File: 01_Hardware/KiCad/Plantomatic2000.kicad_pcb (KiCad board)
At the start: 2 copper layers, 1 part, among them U1 ESP32-WROOM-32E

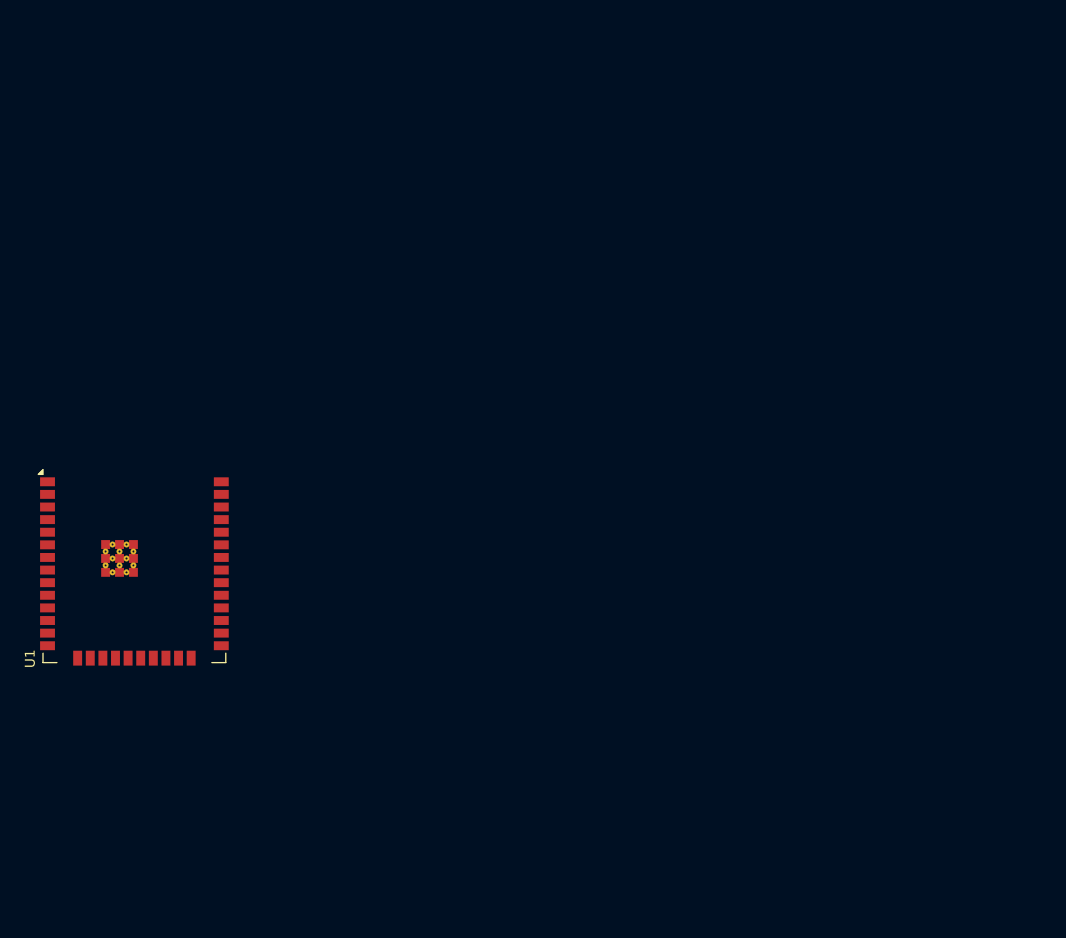
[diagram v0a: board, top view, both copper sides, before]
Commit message: Added foorptrints
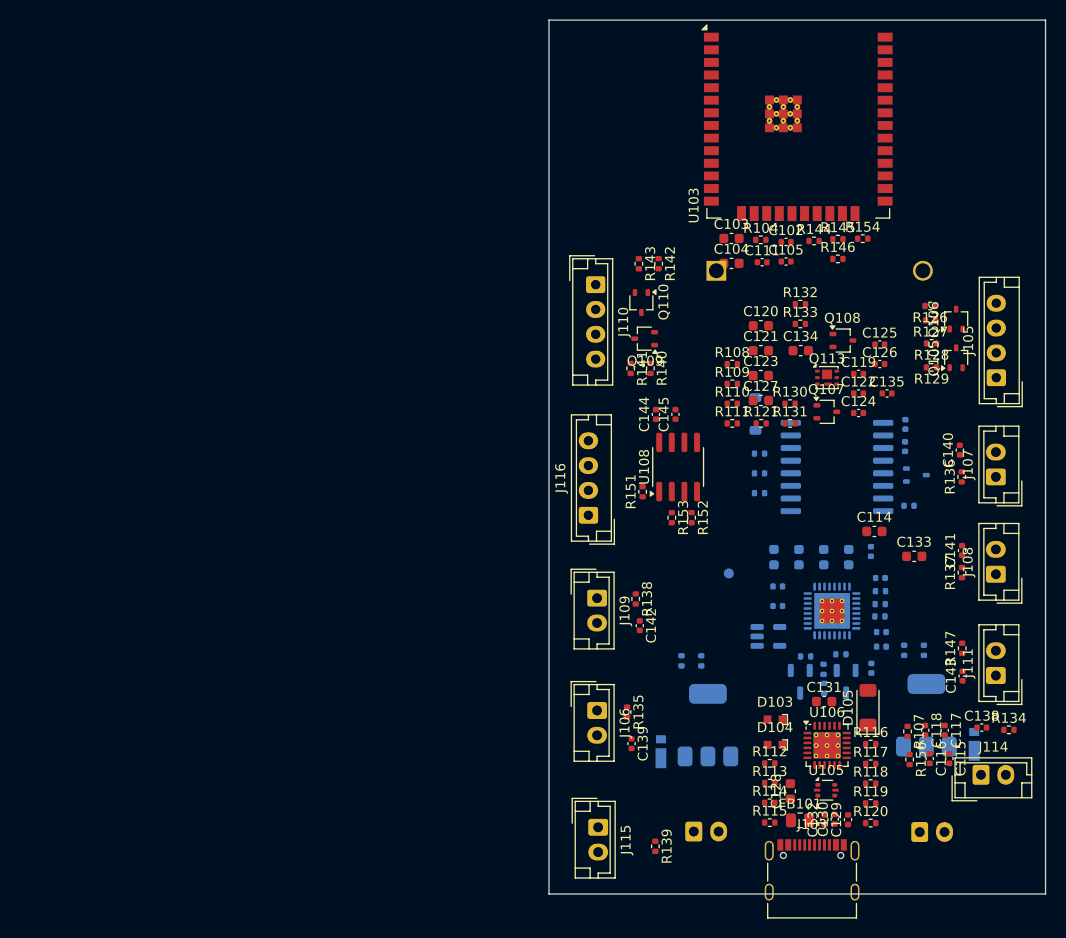
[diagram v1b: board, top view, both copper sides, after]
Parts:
- removed U1: ESP32-WROOM-32E, RF_Module:ESP32-WROOM-32E
- added BT101: Battery_Cell, Battery:BatteryHolder_MYOUNG_BS-07-A1BJ001_CR2032, B.Cu at (197.8, 66.2)
- added C101: 1uF, Capacitor_SMD:C_0402_1005Metric, B.Cu at (213.4, 94.5)
- added C102: 100nF, Capacitor_SMD:C_0402_1005Metric, F.Cu at (204.9, 63.3)
- added C103: 10uF, Capacitor_SMD:C_0603_1608Metric, F.Cu at (199.4, 63.0)
- added C104: 22uF, Capacitor_SMD:C_0603_1608Metric, F.Cu at (199.4, 65.5)
- added C105: 100nF, Capacitor_SMD:C_0402_1005Metric, F.Cu at (204.9, 65.3)
- added C106: 1uF, Capacitor_SMD:C_0402_1005Metric, B.Cu at (214.4, 97.2)
- added C107: 10uF, Capacitor_SMD:C_0603_1608Metric, B.Cu at (203.7, 95.1)
- added C108: 10uF, Capacitor_SMD:C_0603_1608Metric, B.Cu at (206.2, 95.1)
- added C109: 10uF, Capacitor_SMD:C_0603_1608Metric, B.Cu at (208.7, 95.1)
- added C110: 10uF, Capacitor_SMD:C_0603_1608Metric, B.Cu at (211.2, 95.1)
- added C111: 1uF, Capacitor_SMD:C_0402_1005Metric, F.Cu at (202.5, 65.4)
- added C112: 2.2uF, Capacitor_SMD:C_0402_1005Metric, B.Cu at (214.5, 104.1)
- added C113: 100nF, Capacitor_SMD:C_0402_1005Metric, B.Cu at (214.5, 102.6)
- added C114: 1uF, Capacitor_SMD:C_0603_1608Metric, F.Cu at (213.8, 92.5)
- added C115: 100nF, Capacitor_SMD:C_0402_1005Metric, F.Cu at (221.3, 115.4)
- added C116: 100nF, Capacitor_SMD:C_0402_1005Metric, F.Cu at (219.3, 115.4)
- added C117: 100nF, Capacitor_SMD:C_0402_1005Metric, F.Cu at (220.8, 112.5)
- added C118: 100nF, Capacitor_SMD:C_0402_1005Metric, F.Cu at (218.9, 112.5)
- added C119: 100nF, Capacitor_SMD:C_0402_1005Metric, F.Cu at (212.2, 76.6)
- added C120: 47uF, Capacitor_SMD:C_0603_1608Metric, F.Cu at (202.3, 71.8)
- added C121: 47uF, Capacitor_SMD:C_0603_1608Metric, F.Cu at (202.3, 74.3)
- added C122: 100nF, Capacitor_SMD:C_0402_1005Metric, F.Cu at (212.2, 78.6)
- added C123: 10uF, Capacitor_SMD:C_0603_1608Metric, F.Cu at (202.3, 76.8)
- added C124: 100nF, Capacitor_SMD:C_0402_1005Metric, F.Cu at (212.2, 80.6)
- added C125: 58pF, Capacitor_SMD:C_0402_1005Metric, F.Cu at (214.3, 73.7)
- added C126: 4.7nF, Capacitor_SMD:C_0402_1005Metric, F.Cu at (214.3, 75.6)
- added C127: 2.2uF, Capacitor_SMD:C_0603_1608Metric, F.Cu at (202.3, 79.3)
- added C128: 4.7uF, Capacitor_SMD:C_0603_1608Metric, F.Cu at (205.3, 118.7)
- added C129: 100nF, Capacitor_SMD:C_0402_1005Metric, F.Cu at (211.1, 121.5)
- added C130: 100nF, Capacitor_SMD:C_0402_1005Metric, F.Cu at (209.8, 121.5)
- added C131: 4.7uF, Capacitor_SMD:C_0603_1608Metric, F.Cu at (208.7, 109.6)
- added C132: 100nF, Capacitor_SMD:C_0402_1005Metric, F.Cu at (208.7, 121.5)
- added C133: 1uF, Capacitor_SMD:C_0603_1608Metric, F.Cu at (217.8, 95.0)
- added C134: 22uF, Capacitor_SMD:C_0603_1608Metric, F.Cu at (206.3, 74.3)
- added C135: 4.7nF, Capacitor_SMD:C_0402_1005Metric, F.Cu at (215.0, 78.6)
- added C136: 100nF, Capacitor_SMD:C_0402_1005Metric, B.Cu at (216.8, 83.9)
- added C137: 10uF, Capacitor_SMD:C_0402_1005Metric, B.Cu at (216.9, 81.7)
- added C138: 100nF, Capacitor_SMD:C_0402_1005Metric, F.Cu at (224.6, 112.2)
- added C139: 100nF, Capacitor_SMD:C_0402_1005Metric, F.Cu at (189.3, 113.9)
- added C140: 100nF, Capacitor_SMD:C_0402_1005Metric, F.Cu at (222.4, 84.3)
- added C141: 100nF, Capacitor_SMD:C_0402_1005Metric, F.Cu at (222.6, 94.4)
- added C142: 100nF, Capacitor_SMD:C_0402_1005Metric, F.Cu at (190.1, 102.0)
- added C143: 100nF, Capacitor_SMD:C_0402_1005Metric, F.Cu at (222.7, 107.0)
- added C144: 10uF, Capacitor_SMD:C_0402_1005Metric, F.Cu at (191.8, 80.7)
- added C145: 100nF, Capacitor_SMD:C_0402_1005Metric, F.Cu at (193.7, 80.7)
- added C146: 100nF, Capacitor_SMD:C_0402_1005Metric, B.Cu at (213.5, 106.3)
- added C147: 100nF, Capacitor_SMD:C_0402_1005Metric, B.Cu at (204.0, 100.0)
- added C148: 100nF, Capacitor_SMD:C_0402_1005Metric, B.Cu at (204.0, 98.0)
- added D103: LTST-C193KGKT-5A, Custom_Global_Footprints:LTST-C193KGKT-5A, F.Cu at (203.8, 111.4)
- added D104: LTST-C193KGKT-5A, Custom_Global_Footprints:LTST-C193KGKT-5A, F.Cu at (203.8, 114.0)
- added D105: UCLAMP6061P.TNT, Diode_SMD:D_MiniMELF, F.Cu at (213.1, 110.2)
- added D106: 1N4148W, Diode_SMD:D_SOD-123, B.Cu at (201.8, 80.7)
- added D108: SS14, Custom_Global_Footprints:SS14, B.Cu at (192.3, 114.3)
- added D109: SS14, Custom_Global_Footprints:SS14, B.Cu at (223.8, 113.6)
- added FB101: MH2029-300Y, Resistor_SMD:R_0805_2012Metric, F.Cu at (206.3, 121.6)
- added J103: USB_C_Receptacle_USB2.0_16P, Connector_USB:USB_C_Receptacle_Palconn_UTC16-G, F.Cu at (207.5, 126.6)
- added J105: JST_B4B, Connector_JST:JST_EH_B4B-EH-A_1x04_P2.50mm_Vertical, F.Cu at (226.0, 77.0)
- added J106: Line Select, Connector_JST:JST_EH_B2B-EH-A_1x02_P2.50mm_Vertical, F.Cu at (185.8, 110.5)
- added J107: Manual Start, Connector_JST:JST_EH_B2B-EH-A_1x02_P2.50mm_Vertical, F.Cu at (226.0, 87.0)
- added J108: Hour, Connector_JST:JST_EH_B2B-EH-A_1x02_P2.50mm_Vertical, F.Cu at (226.0, 96.8)
- added J109: Minute, Connector_JST:JST_EH_B2B-EH-A_1x02_P2.50mm_Vertical, F.Cu at (185.8, 99.2)
- added J110: JST_4B4, Connector_JST:JST_EH_B4B-EH-A_1x04_P2.50mm_Vertical, F.Cu at (185.7, 67.6)
- added J111: System Reset, Connector_JST:JST_EH_B2B-EH-A_1x02_P2.50mm_Vertical, F.Cu at (226.0, 107.0)
- added J112: JST_B2B, Connector_JST:JST_EH_B2B-EH-A_1x02_P2.50mm_Vertical, B.Cu at (195.6, 122.7)
- added J113: JST_B2B, Connector_JST:JST_EH_B2B-EH-A_1x02_P2.50mm_Vertical, B.Cu at (218.3, 122.8)
- added J114: System Wake Up, Connector_JST:JST_EH_B2B-EH-A_1x02_P2.50mm_Vertical, F.Cu at (224.5, 117.0)
- added J115: Running LED, Connector_JST:JST_EH_B2B-EH-A_1x02_P2.50mm_Vertical, F.Cu at (185.9, 122.3)
- added J116: JST_4B4, Connector_JST:JST_EH_B4B-EH-A_1x04_P2.50mm_Vertical, F.Cu at (185.0, 90.9)
- added Q101: IRLL014NTRPBF, Package_TO_SOT_SMD:SOT-223, B.Cu at (219.0, 111.0)
- added Q102: IRLL014NTRPBF, Package_TO_SOT_SMD:SOT-223, B.Cu at (197.0, 112.0)
- added Q104: NVTA7002NT1G, Package_TO_SOT_SMD:SOT-323_SC-70, B.Cu at (218.0, 86.8)
- added Q105: RU1E002SPTCL, Package_TO_SOT_SMD:SOT-323_SC-70, F.Cu at (222.0, 75.0)
- added Q106: NVTA7002NT1G, Package_TO_SOT_SMD:SOT-323_SC-70, F.Cu at (222.0, 71.1)
- added Q107: NVTA7002NT1G, Package_TO_SOT_SMD:SOT-323_SC-70, F.Cu at (209.0, 80.4)
- added Q108: RU1E002SPTCL, Package_TO_SOT_SMD:SOT-323_SC-70, F.Cu at (210.6, 73.3)
- added Q109: NVTA7002NT1G, Package_TO_SOT_SMD:SOT-323_SC-70, F.Cu at (190.6, 73.1)
- added Q110: RU1E002SPTCL, Package_TO_SOT_SMD:SOT-323_SC-70, F.Cu at (190.3, 69.4)
- added Q111: DTC143Z, Package_TO_SOT_SMD:SOT-23-3, B.Cu at (206.3, 107.6)
- added Q112: DTC143Z, Package_TO_SOT_SMD:SOT-23-3, B.Cu at (210.9, 107.6)
- added Q113: CSD17313Q2, Package_SON:Texas_DQK, F.Cu at (209.0, 77.0)
- added R102: 470R, Resistor_SMD:R_0402_1005Metric, B.Cu at (218.8, 104.5)
- added R103: 10K, Resistor_SMD:R_0402_1005Metric, B.Cu at (216.8, 104.5)
- added R104: 10K, Resistor_SMD:R_0402_1005Metric, F.Cu at (202.3, 63.1)
- added R105: 470R, Resistor_SMD:R_0402_1005Metric, B.Cu at (194.3, 105.5)
- added R106: 10K, Resistor_SMD:R_0402_1005Metric, B.Cu at (196.3, 105.5)
- added R107: 470R, Resistor_SMD:R_0402_1005Metric, F.Cu at (217.1, 112.6)
- added R108: 158K, Resistor_SMD:R_0402_1005Metric, F.Cu at (199.5, 75.6)
- added R109: 14K3, Resistor_SMD:R_0402_1005Metric, F.Cu at (199.5, 77.6)
- added R110: 10K, Resistor_SMD:R_0402_1005Metric, F.Cu at (199.5, 79.6)
- added R111: 40K, Resistor_SMD:R_0402_1005Metric, F.Cu at (199.5, 81.6)
- added R112: 1K, Resistor_SMD:R_0402_1005Metric, F.Cu at (203.2, 115.8)
- added R113: 22K1, Resistor_SMD:R_0402_1005Metric, F.Cu at (203.2, 117.8)
- added R114: 470R, Resistor_SMD:R_0402_1005Metric, F.Cu at (203.2, 119.8)
- added R115: 470R, Resistor_SMD:R_0402_1005Metric, F.Cu at (203.2, 121.8)
- added R116: 5K1, Resistor_SMD:R_0402_1005Metric, F.Cu at (213.4, 113.9)
- added R117: 47K5, Resistor_SMD:R_0402_1005Metric, F.Cu at (213.4, 115.9)
- added R118: 5K1, Resistor_SMD:R_0402_1005Metric, F.Cu at (213.4, 117.9)
- added R119: 1K, Resistor_SMD:R_0402_1005Metric, F.Cu at (213.4, 119.9)
- added R120: 1K, Resistor_SMD:R_0402_1005Metric, F.Cu at (213.4, 121.9)
- added R121: 10K, Resistor_SMD:R_0402_1005Metric, F.Cu at (202.4, 81.6)
- added R122: 220R, Resistor_SMD:R_0402_1005Metric, B.Cu at (202.2, 88.6)
- added R123: 470R, Resistor_SMD:R_0402_1005Metric, B.Cu at (202.2, 86.6)
- added R124: 10K, Resistor_SMD:R_0402_1005Metric, B.Cu at (202.2, 84.7)
- added R125: 470R, Resistor_SMD:R_0402_1005Metric, B.Cu at (217.2, 89.9)
- added R126: 10K, Resistor_SMD:R_0402_1005Metric, F.Cu at (219.4, 69.8)
- added R127: 470R, Resistor_SMD:R_0402_1005Metric, F.Cu at (219.4, 71.2)
- added R128: 470R, Resistor_SMD:R_0402_1005Metric, F.Cu at (219.5, 73.6)
- added R129: 10K, Resistor_SMD:R_0402_1005Metric, F.Cu at (219.5, 76.0)
- added R130: 10K, Resistor_SMD:R_0402_1005Metric, F.Cu at (205.3, 79.6)
- added R131: 470R, Resistor_SMD:R_0402_1005Metric, F.Cu at (205.3, 81.6)
- added R132: 10K, Resistor_SMD:R_0402_1005Metric, F.Cu at (206.3, 69.6)
- added R133: 10K, Resistor_SMD:R_0402_1005Metric, F.Cu at (206.3, 71.6)
- added R134: 0R, Resistor_SMD:R_0402_1005Metric, F.Cu at (227.3, 112.5)
- added R135: 0R, Resistor_SMD:R_0402_1005Metric, F.Cu at (188.9, 110.7)
- added R136: 0R, Resistor_SMD:R_0402_1005Metric, F.Cu at (222.6, 87.0)
- added R137: 0R, Resistor_SMD:R_0402_1005Metric, F.Cu at (222.6, 96.6)
- added R138: 0R, Resistor_SMD:R_0402_1005Metric, F.Cu at (189.7, 99.3)
- added R139: 470R, Resistor_SMD:R_0402_1005Metric, F.Cu at (191.7, 124.2)
- added R140: 10K, Resistor_SMD:R_0402_1005Metric, F.Cu at (191.2, 76.1)
- added R141: 470R, Resistor_SMD:R_0402_1005Metric, F.Cu at (189.2, 76.1)
- added R142: 10K, Resistor_SMD:R_0402_1005Metric, F.Cu at (192.0, 65.5)
- added R143: 470R, Resistor_SMD:R_0402_1005Metric, F.Cu at (190.1, 65.5)
- added R144: 4K7, Resistor_SMD:R_0402_1005Metric, F.Cu at (207.7, 63.2)
- added R145: 4K7, Resistor_SMD:R_0402_1005Metric, F.Cu at (210.1, 63.1)
- added R146: 0R, Resistor_SMD:R_0402_1005Metric, F.Cu at (210.1, 65.0)
- added R147: 0R, Resistor_SMD:R_0402_1005Metric, F.Cu at (222.6, 104.3)
- added R148: 220R, Resistor_SMD:R_0402_1005Metric, B.Cu at (214.3, 101.0)
- added R149: 220R, Resistor_SMD:R_0402_1005Metric, B.Cu at (214.3, 99.8)
- added R150: 220R, Resistor_SMD:R_0402_1005Metric, B.Cu at (214.4, 98.5)
- added R151: 4K7, Resistor_SMD:R_0402_1005Metric, F.Cu at (190.4, 88.5)
- added R152: 4K7, Resistor_SMD:R_0402_1005Metric, F.Cu at (195.4, 91.1)
- added R153: 4K7, Resistor_SMD:R_0402_1005Metric, F.Cu at (193.4, 91.1)
- added R154: 10K, Resistor_SMD:R_0402_1005Metric, F.Cu at (212.6, 63.0)
- added R155: 12K, Resistor_SMD:R_0402_1005Metric, B.Cu at (206.8, 105.1)
- added R156: 470R, Resistor_SMD:R_0402_1005Metric, F.Cu at (217.3, 115.5)
- added R157: 12K, Resistor_SMD:R_0402_1005Metric, B.Cu at (208.6, 106.4)
- added R158: 12K, Resistor_SMD:R_0402_1005Metric, B.Cu at (208.7, 108.3)
- added R159: 5K1, Resistor_SMD:R_0402_1005Metric, B.Cu at (210.4, 104.9)
- added TP101: +VBAT, TestPoint:TestPoint_Pad_D1.0mm, B.Cu at (199.1, 96.7)
- added U101: XC6220B331MR, Package_TO_SOT_SMD:SOT-23-5, B.Cu at (203.1, 103.1)
- added U102: nPM1300, Package_DFN_QFN:QFN-32-1EP_5x5mm_P0.5mm_EP3.6x3.6mm_ThermalVias, B.Cu at (209.5, 100.5)
- added U103: ESP32-WROOM-32E, RF_Module:ESP32-WROOM-32E, F.Cu at (206.1, 48.0)
- added U105: USBLC6-2P6, Package_TO_SOT_SMD:SOT-666, F.Cu at (208.9, 118.5)
- added U106: CP2102N-A02-GQFN24, Package_DFN_QFN:QFN-24-1EP_4x4mm_P0.5mm_EP2.7x2.6mm_ThermalVias, F.Cu at (209.0, 114.0)
- added U107: DS3231M, Package_SO:SOIC-16W_7.5x10.3mm_P1.27mm, B.Cu at (210.0, 86.0)
- added U108: AT24CS01-SSHM, Package_SO:SOIC-8_3.9x4.9mm_P1.27mm, F.Cu at (194.0, 86.0)
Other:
- board outline added: 50 x 88 mm

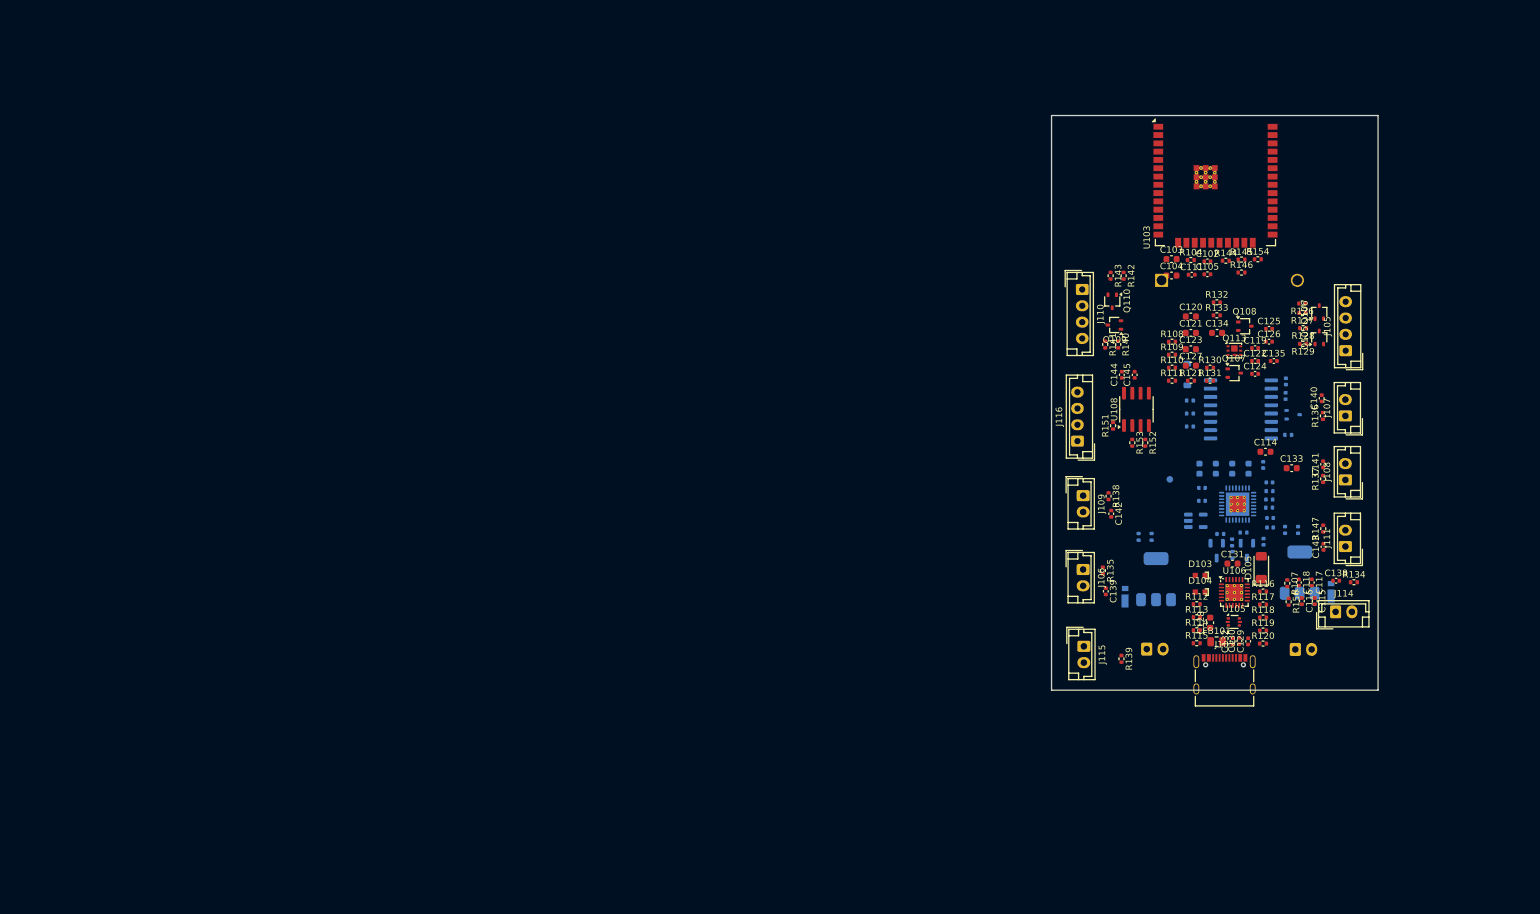
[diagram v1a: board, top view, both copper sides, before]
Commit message: Finised assigning footprints
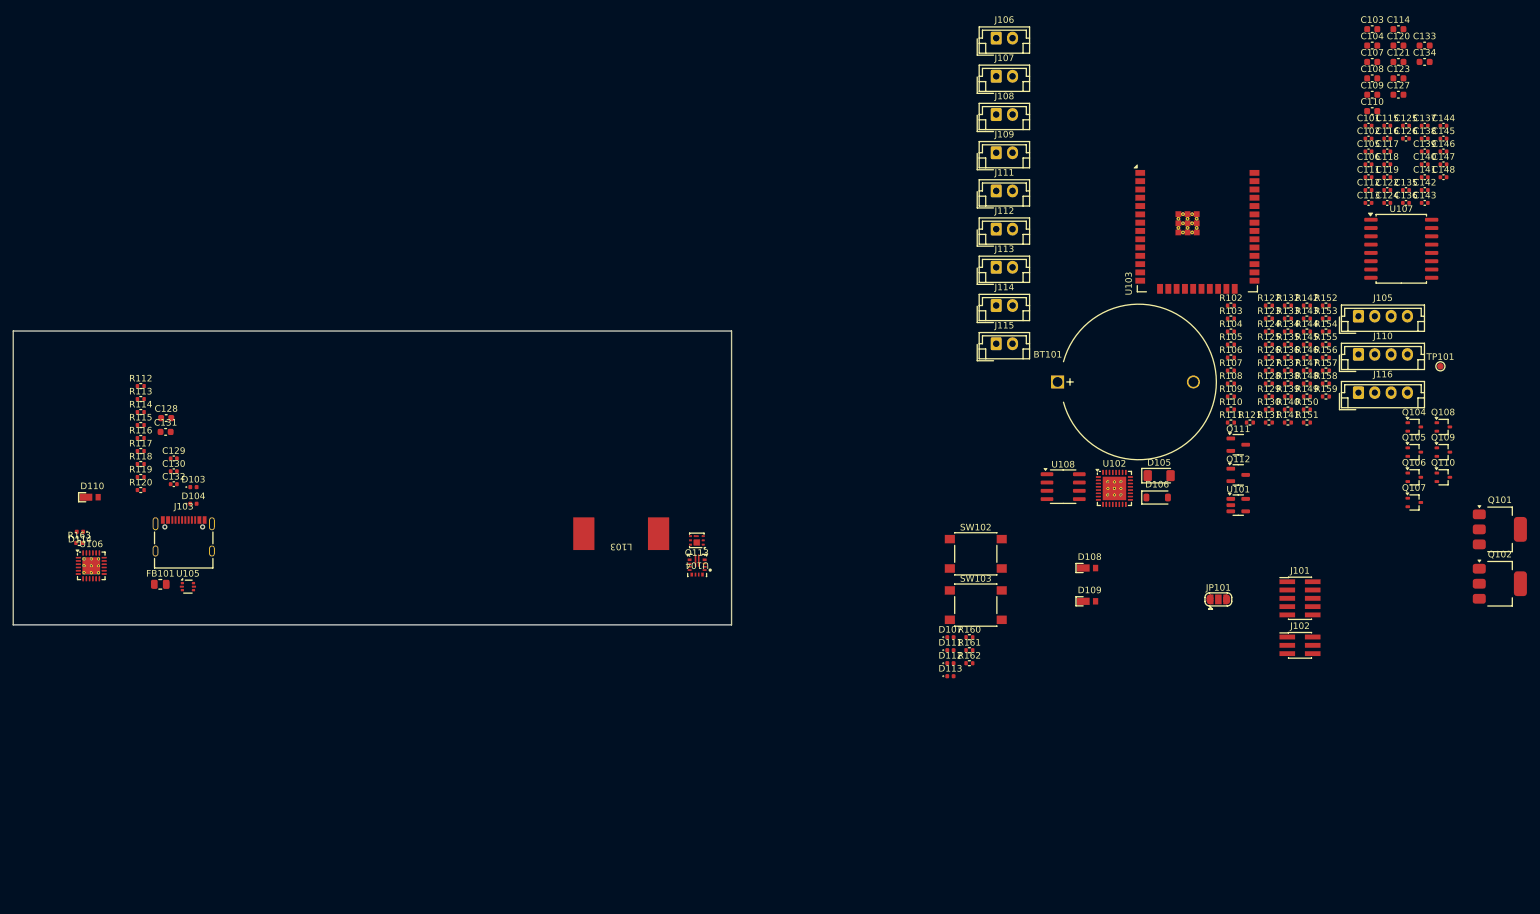
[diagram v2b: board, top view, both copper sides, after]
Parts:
- added D107: SML-P12U2TT86R, LED_SMD:LED_0402_1005Metric, F.Cu at (165.5, 120.9)
- added D110: SS14, Custom_Global_Footprints:SS14M_Flyback_Diode, F.Cu at (34.1, 99.5)
- added D111: SML-P12U2TT86R, LED_SMD:LED_0402_1005Metric, F.Cu at (165.5, 122.9)
- added D112: SML-P12U2TT86R, LED_SMD:LED_0402_1005Metric, F.Cu at (165.5, 124.9)
- added D113: SML-P12U2TT86R, LED_SMD:LED_0402_1005Metric, F.Cu at (165.5, 126.9)
- added D114: SML-P12U2TT86R, LED_SMD:LED_0402_1005Metric, F.Cu at (32.2, 104.7)
- added J101: Conn_02x05_Odd_Even, Connector_PinHeader_1.27mm:PinHeader_2x05_P1.27mm_Vertical_SMD, F.Cu at (219.1, 114.9)
- added J102: Conn_02x03_Odd_Even, Connector_PinHeader_1.27mm:PinHeader_2x03_P1.27mm_Vertical_SMD, F.Cu at (219.1, 122.1)
- added JP101: ModSel, Jumper:SolderJumper-3_P1.3mm_Open_RoundedPad1.0x1.5mm, F.Cu at (206.6, 115.1)
- added L103: 4.7uH (SPM12565VT-4R7M-D), Custom_Global_Footprints:SPM12565VT-4R7M, F.Cu at (115.1, 105.0)
- added R160: 1K, Resistor_SMD:R_0402_1005Metric, F.Cu at (168.4, 120.9)
- added R161: 1K, Resistor_SMD:R_0402_1005Metric, F.Cu at (168.4, 122.9)
- added R162: 1K, Resistor_SMD:R_0402_1005Metric, F.Cu at (168.4, 124.9)
- added R163: 1K, Resistor_SMD:R_0402_1005Metric, F.Cu at (32.1, 106.5)
- added SW102: SW_Push, Button_Switch_SMD:SW_SPST_PTS645, F.Cu at (169.4, 108.1)
- added SW103: SW_Push, Button_Switch_SMD:SW_SPST_PTS645, F.Cu at (169.4, 116.0)
- added U104: TPS61287, Custom_Global_Footprints:RZP0014A-MFG, F.Cu at (126.7, 109.9)
- BT101, C101, C106, C107, C108, C109, C110, C112, C113, C136, C137, C146, C147, C148, D106, J112, J113, Q104, Q111, Q112, R102, R103, R105, R106, R122, R124, R125, R148, R149, R150, R155, R157, R158, R159, TP101, U101, U102, U107: moved to F.Cu
- D103, D104: value LTST-C193KGKT-5A -> SML-P13PTT86R; footprint Custom_Global_Footprints:LTST-C193KGKT-5A -> LED_SMD:LED_0402_1005Metric
- D108, D109: footprint Custom_Global_Footprints:SS14 -> Custom_Global_Footprints:SS14M_Flyback_Diode; moved to F.Cu
- Q101, Q102: value IRLL014NTRPBF -> IRLL014NP; moved to F.Cu
- R123: value 470R -> 1K; moved to F.Cu
- R128, R143: value 470R -> 10K
- moved U106 175.1 mm to (34.0, 110.0)
- moved R116 173.5 mm to (41.5, 90.4)
- moved R117 173.5 mm to (41.5, 92.4)
- moved R118 173.5 mm to (41.5, 94.4)
- moved R119 173.5 mm to (41.5, 96.4)
- moved R120 173.5 mm to (41.5, 98.3)
- moved C129 166.9 mm to (46.6, 93.5), turned to 0 degrees
- moved C130 165.2 mm to (46.6, 95.5), turned to 0 degrees
- moved R112 165.1 mm to (41.5, 82.4)
- moved R113 165.1 mm to (41.5, 84.4)
- moved R114 165.1 mm to (41.5, 86.4)
- moved R115 165.1 mm to (41.5, 88.4)
- moved C131 164.6 mm to (45.3, 89.5)
- moved C132 163.9 mm to (46.6, 97.5), turned to 0 degrees
- moved C128 162.9 mm to (45.4, 87.3), turned to 0 degrees
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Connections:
- Q101 pad 4: (no net) -> Net-(D108-A)
- Q102 pad 4: (no net) -> Net-(D109-A)
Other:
- board size 50 x 88 mm -> 110 x 45 mm
